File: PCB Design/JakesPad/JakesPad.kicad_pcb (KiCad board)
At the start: 2 copper layers, 277 x 171 mm, 39 parts, among them SW1 SW_Push, SW2 SW_Push, SW3 SW_Push, SW4 SW_Push, SW5 SW_Push, SW6 SW_Push, U2 rp2040-zero

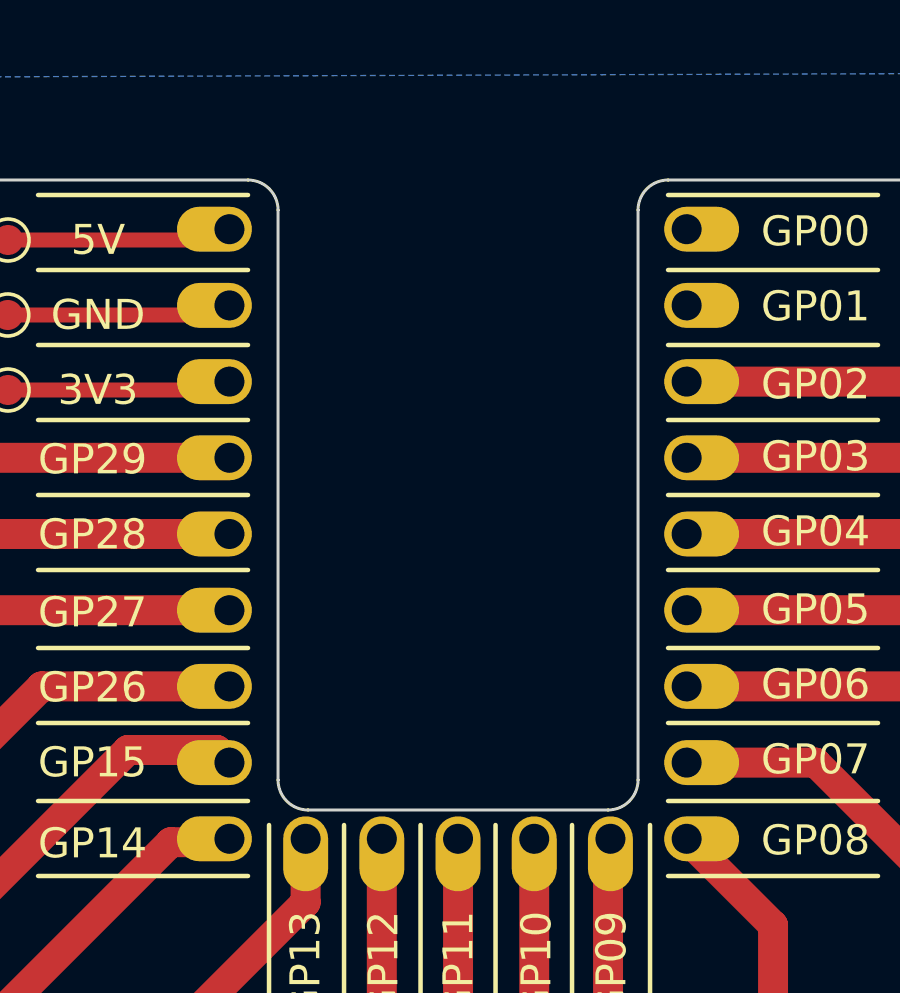
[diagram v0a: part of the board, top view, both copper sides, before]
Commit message: Need to update component placement and add RGB.
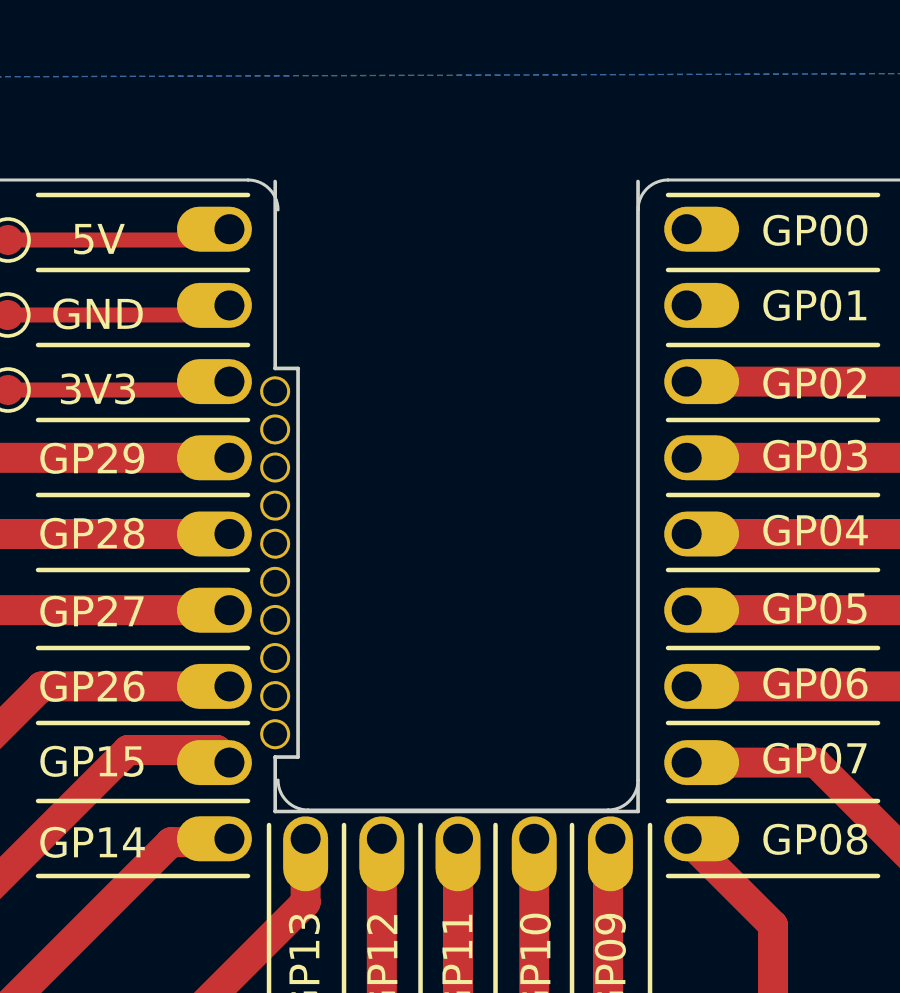
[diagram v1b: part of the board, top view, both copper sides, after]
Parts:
- U2: footprint mcu:rp2040-zero-tht -> mcu:rp2040-zero-tht-pads-cutout
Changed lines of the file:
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@@
     )
   )
-  (footprint "mcu:rp2040-zero-tht" (layer "F.Cu")
+  (footprint "mcu:rp2040-zero-tht-pads-cutout" (layer "F.Cu")
     (at 222 66.3)
     (property "Sheetfile" "JakesPad.kicad_sch")
@@
         (effects (font (size 0.6096 0.6096) (thickness 0.0762)))
     )
-    (fp_line (start -6 -11.75) (end -6 9.25)
-      (stroke (width 0.12) (type solid)) (layer "Dwgs.User"))
-    (fp_line (start -6 9.25) (end 6 9.25)
-      (stroke (width 0.12) (type solid)) (layer "Dwgs.User"))
-    (fp_line (start 6 9.25) (end 6 -11.75)
-      (stroke (width 0.12) (type solid)) (layer "Dwgs.User"))
     (fp_rect (start -9 -11.75) (end 9 11.75)
       (stroke (width 0.12) (type solid)) (fill none) (layer "Dwgs.User"))
+    (fp_line (start -6.096 -5.518) (end -6.096 -11.75)
+      (stroke (width 0.12) (type solid)) (layer "Edge.Cuts"))
+    (fp_line (start -6.096 7.436) (end -5.334 7.436)
+      (stroke (width 0.12) (type solid)) (layer "Edge.Cuts"))
+    (fp_line (start -6.096 9.25) (end -6.096 7.436)
+      (stroke (width 0.12) (type solid)) (layer "Edge.Cuts"))
+    (fp_line (start -6.096 9.25) (end 6 9.25)
+      (stroke (width 0.12) (type solid)) (layer "Edge.Cuts"))
+    (fp_line (start -5.334 -5.518) (end -6.096 -5.518)
+      (stroke (width 0.12) (type solid)) (layer "Edge.Cuts"))
+    (fp_line (start -5.334 7.436) (end -5.334 -5.518)
+      (stroke (width 0.12) (type solid)) (layer "Edge.Cuts"))
+    (fp_line (start 6 9.25) (end 6 -11.75)
+      (stroke (width 0.12) (type solid)) (layer "Edge.Cuts"))
     (pad "1" thru_hole oval (at 7.62 -10.16 180) (size 2.5 1.5) (drill 1 (offset -0.5 0)) (layers "*.Cu" "*.Mask")
       (net 2 "unconnected-(U2-0-Pad1)") (pinfunction "0") (pintype "bidirectional+no_connect"))
@@
     (pad "23" thru_hole oval (at -7.62 -10.16) (size 2.5 1.5) (drill 1 (offset -0.5 0)) (layers "*.Cu" "*.Mask")
       (net 24 "+5V") (pinfunction "5V") (pintype "power_out"))
-    (model "${KIPRJMOD}/CAD Renders/rp2040-zero-2.snapshot.6/RP2040-ZERO-WAVESHARE without headers.STEP"
-      (offset (xyz 0 0 0))
-      (scale (xyz 1 1 1))
-      (rotate (xyz -90 0 0))
-    )
+    (pad "24" thru_hole circle (at -6.096 6.674) (size 1 1) (drill 0.8) (layers "*.Cu" "*.Mask"))
+    (pad "25" thru_hole circle (at -6.096 5.404) (size 1 1) (drill 0.8) (layers "*.Cu" "*.Mask"))
+    (pad "26" thru_hole circle (at -6.096 4.134) (size 1 1) (drill 0.8) (layers "*.Cu" "*.Mask"))
+    (pad "27" thru_hole circle (at -6.096 2.864) (size 1 1) (drill 0.8) (layers "*.Cu" "*.Mask"))
+    (pad "28" thru_hole circle (at -6.096 1.594) (size 1 1) (drill 0.8) (layers "*.Cu" "*.Mask"))
+    (pad "29" thru_hole circle (at -6.096 0.324) (size 1 1) (drill 0.8) (layers "*.Cu" "*.Mask"))
+    (pad "30" thru_hole circle (at -6.096 -0.946) (size 1 1) (drill 0.8) (layers "*.Cu" "*.Mask"))
+    (pad "31" thru_hole circle (at -6.096 -2.216) (size 1 1) (drill 0.8) (layers "*.Cu" "*.Mask"))
+    (pad "32" thru_hole circle (at -6.096 -3.486) (size 1 1) (drill 0.8) (layers "*.Cu" "*.Mask"))
+    (pad "33" thru_hole circle (at -6.096 -4.756) (size 1 1) (drill 0.8) (layers "*.Cu" "*.Mask"))
   )
   (footprint "keyswitches.pretty-master:Kailh_socket_PG1350_optional" (layer "F.Cu")
@@
   (gr_line (start 360.5 60) (end 360.5 220)
     (stroke (width 0.1) (type default)) (layer "Edge.Cuts"))
-  (gr_line (start 216 55.5) (end 216 74.5)
-    (stroke (width 0.1) (type default)) (layer "Edge.Cuts"))
   (gr_arc (start 217 75.5) (mid 216.292893 75.207107) (end 216 74.5)
